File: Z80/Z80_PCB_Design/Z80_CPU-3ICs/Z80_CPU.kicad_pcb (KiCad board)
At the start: 2 copper layers, 95 x 95 mm, 49 parts, among them J1 USB_B, J2 Conn_01x12, J3 Conn_01x12, J4 Conn_01x02, J5 Conn_02x20_Odd_Even, U1 Z80CPU, U2 AS6C4008, U3 4.9152 MHz, U4 CY8C5267AXI-LP051, U5 MCP23017_SP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

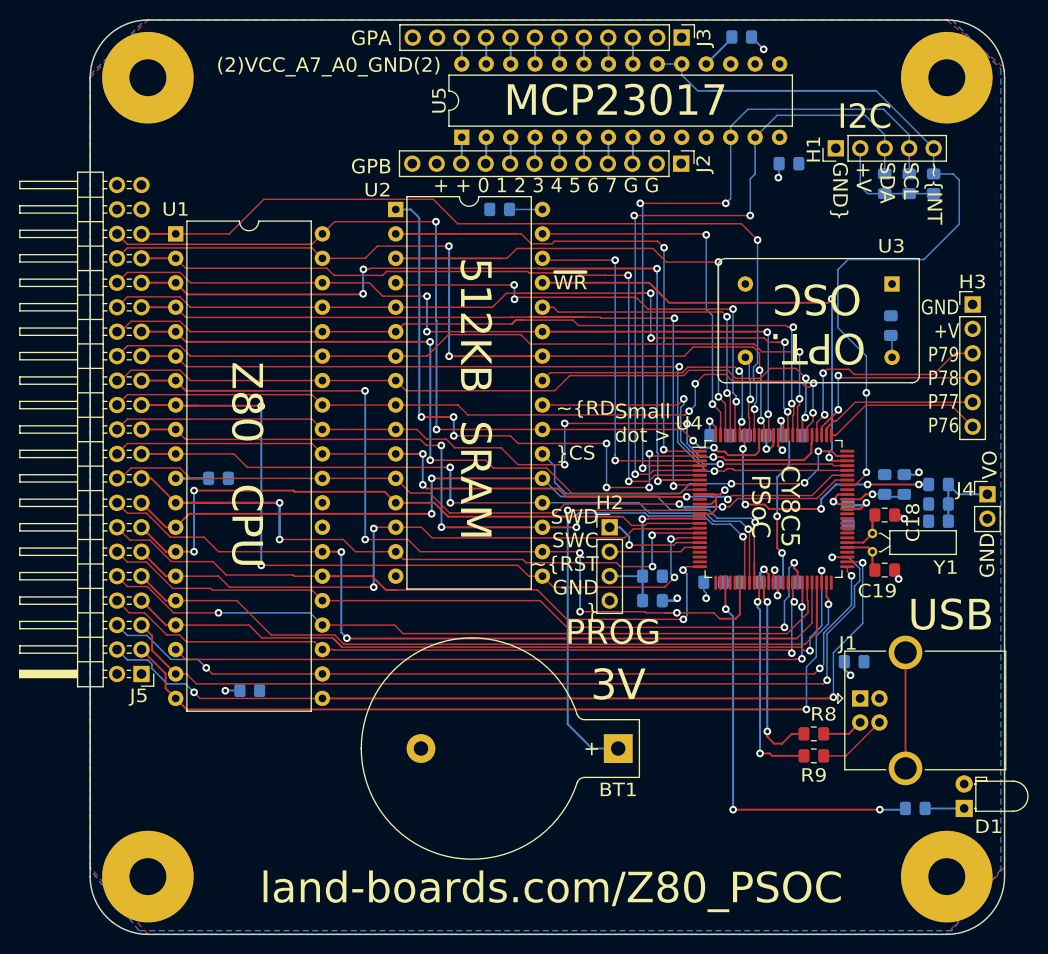
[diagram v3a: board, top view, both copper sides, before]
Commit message: Add 4 pin connector to spare PSoC pins
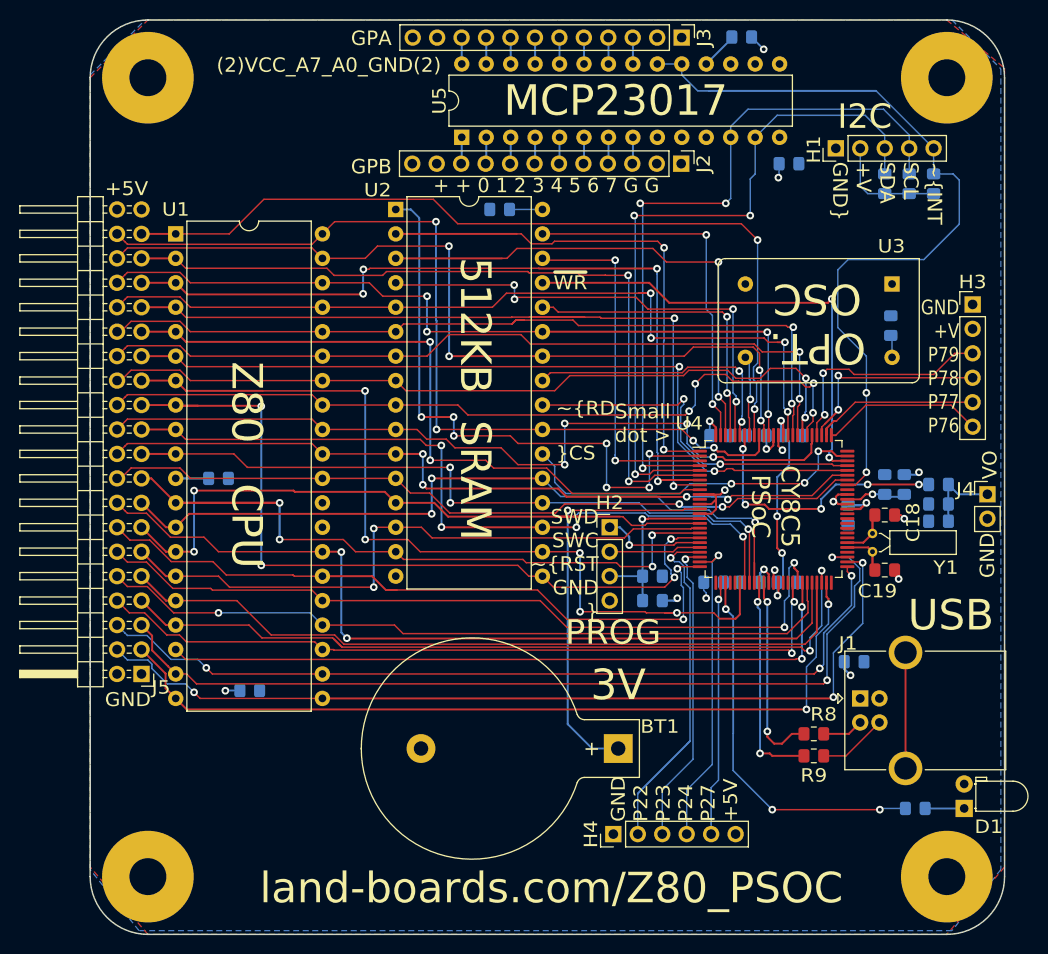
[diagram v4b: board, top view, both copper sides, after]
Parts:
- added H4: Conn_01x06, Connector_PinHeader_2.54mm:PinHeader_1x06_P2.54mm_Vertical, F.Cu at (54.4, 84.6)
- J5: footprint Connector_PinHeader_2.54mm:PinHeader_2x21_P2.54mm_Horizontal -> Connector_PinHeader_2.54mm:PinHeader_2x20_P2.54mm_Horizontal
- L1: value ChipInd -> HZ0805E601R-10
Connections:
- U4 pad 22: (no net) -> /P22
- U4 pad 23: (no net) -> /P23
- U4 pad 24: (no net) -> /P24
- U4 pad 27: (no net) -> /P27
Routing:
- net /P22: track 0.00 -> 43.5 mm, vias 0 -> 1
- net /P24: track 0.00 -> 32.5 mm, vias 0 -> 1
- net /P23: track 0.00 -> 31.9 mm, vias 0 -> 1
- net /P27: track 0.00 -> 26.5 mm, vias 0 -> 1
- net Net-(R7-Pad2): track 41.9 -> 39.5 mm
- net /~CPURST: track 70.1 -> 70.7 mm
- net /CPUD3: track 80.5 -> 81.0 mm
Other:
- board text added: "+5V"
- board text added: "GND P22 P23 P24 P27 +5V"
